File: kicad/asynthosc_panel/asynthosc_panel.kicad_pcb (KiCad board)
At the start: 2 copper layers, 71.1 x 128.4 mm, 0 parts

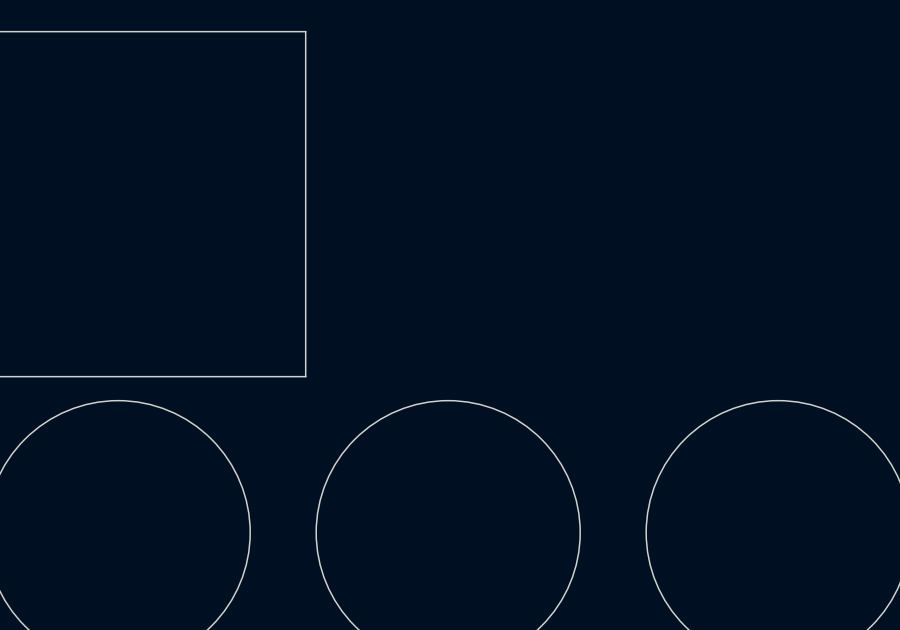
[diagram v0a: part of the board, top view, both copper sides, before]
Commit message: Refine asynthosc panel artwork
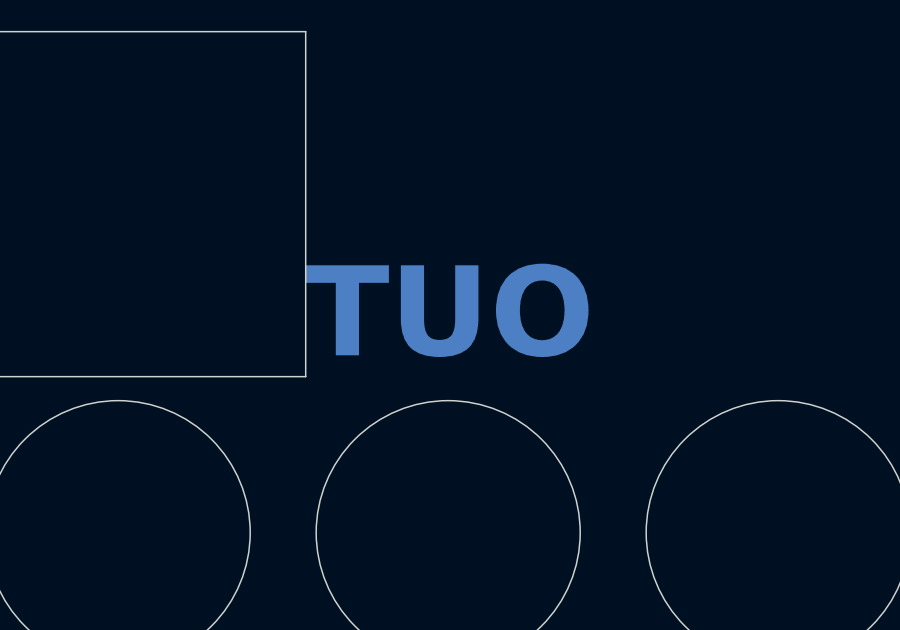
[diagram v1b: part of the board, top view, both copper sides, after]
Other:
- board text added: "1"
- board text added: "2"
- board text added: "3"
- board text added: "4"
- board text added: "MIDI"
- board text added: "OUT"
- board text added: "T1"
- board text added: "T2"
- board text added: "aSynth2OSC"
- board text removed: "This actually is front"
